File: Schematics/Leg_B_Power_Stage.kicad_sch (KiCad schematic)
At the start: 40 parts, among them Q4 C3M0025065K, Q5 C3M0025065K, U3 UCC21710QDWRQ1, U4 UCC21710QDWRQ1

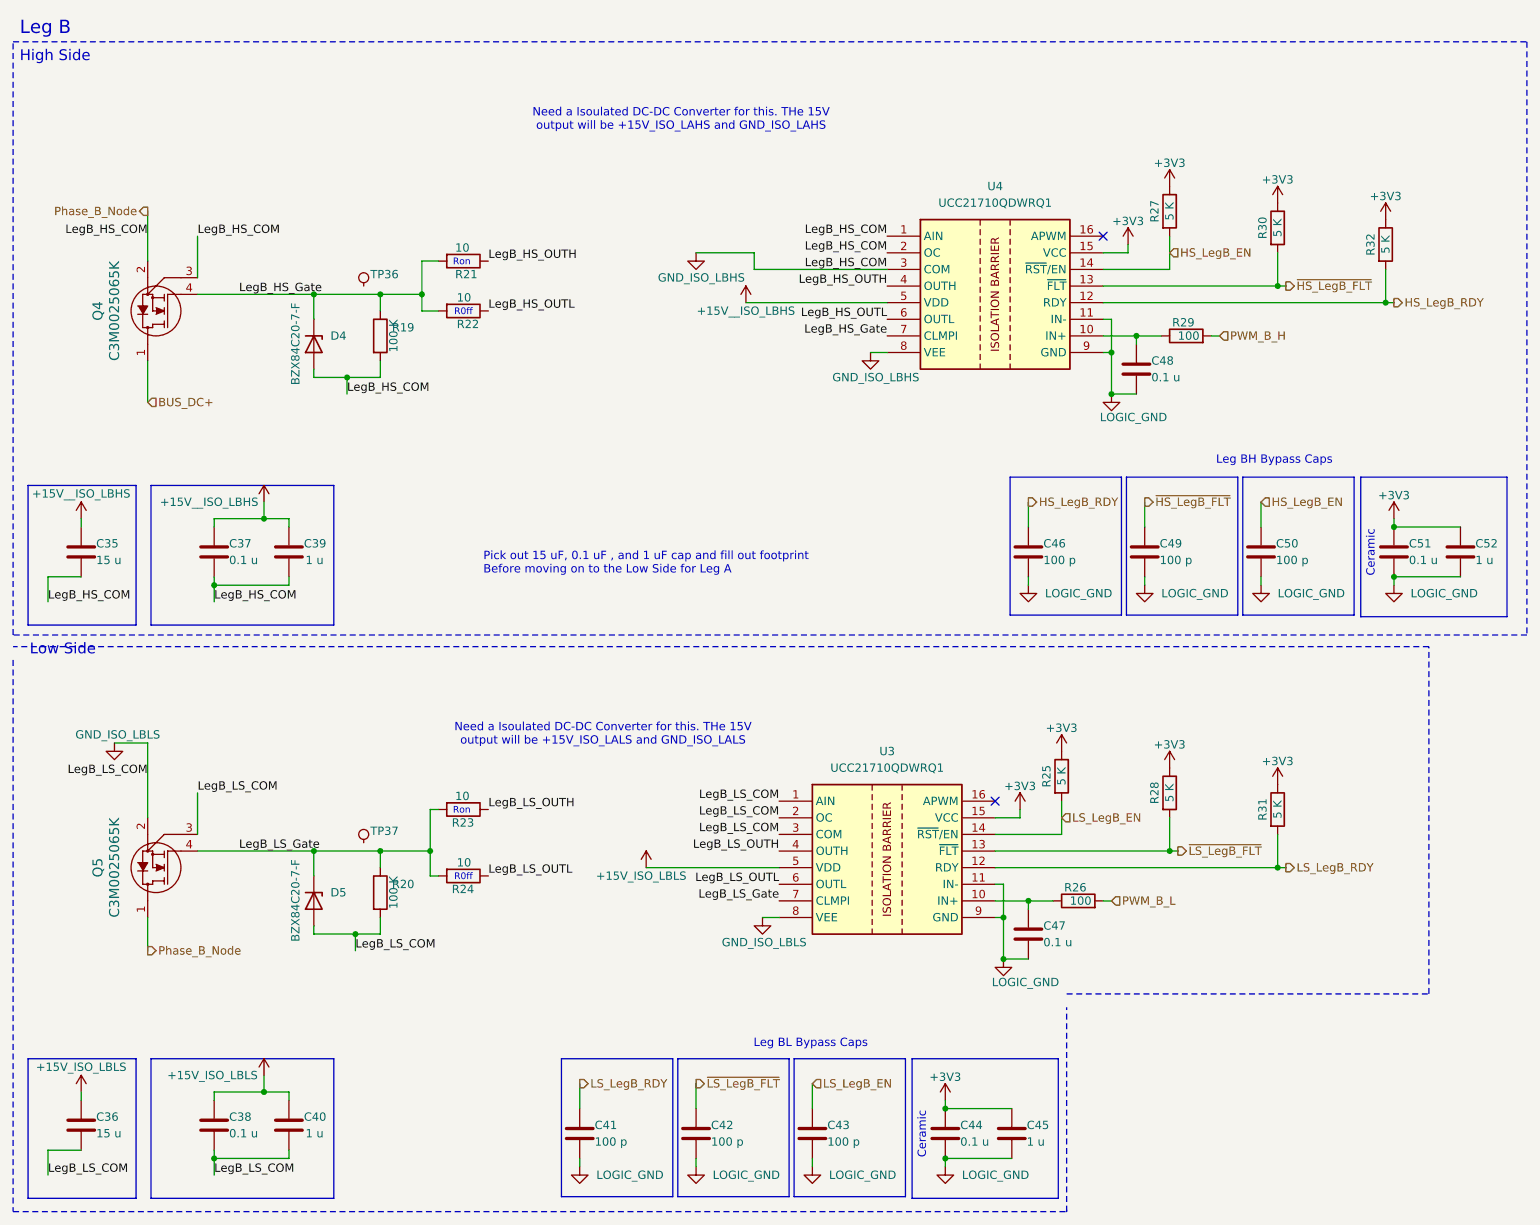
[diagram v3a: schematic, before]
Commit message: Changing units on all Caps to display xF
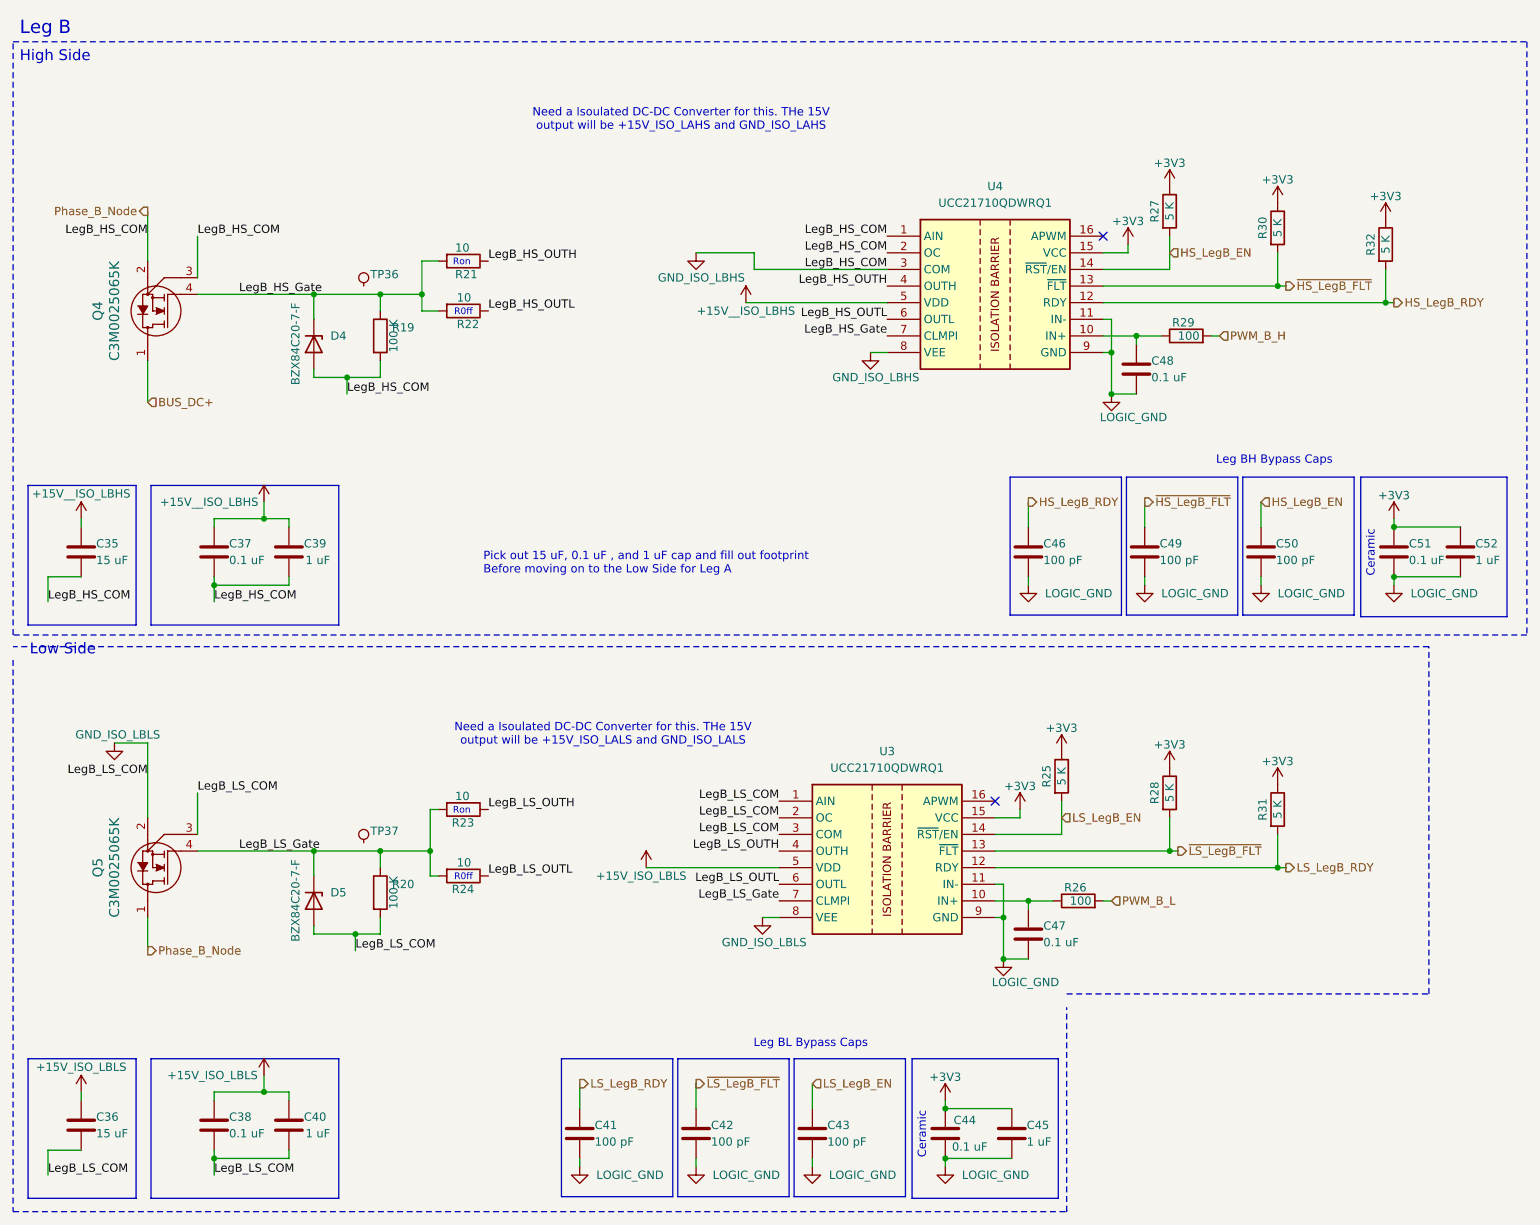
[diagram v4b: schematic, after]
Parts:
- C35, C36: value 15 u -> 15 uF
- C37, C38, C44, C47, C48, C51: value 0.1 u -> 0.1 uF
- C39, C40, C45, C52: value 1 u -> 1 uF
- C41, C42, C43, C46, C49, C50: value 100 p -> 100 pF
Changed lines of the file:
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@@
 	(rectangle
 		(start 34.798 83.82)
-		(end 62.738 105.156)
+		(end 63.5 105.156)
 		(stroke
 			(width 0)
@@
 	(rectangle
 		(start 34.798 171.45)
-		(end 62.738 192.786)
+		(end 63.5 192.786)
 		(stroke
 			(width 0)
@@
 			)
 		)
-		(property "Value" "100 p"
+		(property "Value" "100 pF"
 			(at 138.176 184.15 0)
 			(effects
@@
 			)
 		)
-		(property "Value" "100 p"
+		(property "Value" "100 pF"
 			(at 171.196 95.25 0)
 			(effects
@@
 			)
 		)
-		(property "Value" "15 u"
+		(property "Value" "15 uF"
 			(at 26.416 182.88 0)
 			(effects
@@
 			)
 		)
-		(property "Value" "0.1 u"
+		(property "Value" "0.1 uF"
 			(at 46.736 95.25 0)
 			(effects
@@
 			)
 		)
-		(property "Value" "100 p"
+		(property "Value" "100 pF"
 			(at 206.756 95.25 0)
 			(effects
@@
 			)
 		)
-		(property "Value" "1 u"
+		(property "Value" "1 uF"
 			(at 168.656 184.15 0)
 			(effects
@@
 			)
 		)
-		(property "Value" "1 u"
+		(property "Value" "1 uF"
 			(at 58.42 95.25 0)
 			(effects
@@
 		(dnp no)
 		(property "Reference" "C44"
-			(at 158.496 181.61 0)
+			(at 157.48 180.848 0)
 			(effects
 				(font
@@
 			)
 		)
-		(property "Value" "0.1 u"
-			(at 158.496 184.15 0)
+		(property "Value" "0.1 uF"
+			(at 157.226 184.912 0)
 			(effects
 				(font
@@
 			)
 		)
-		(property "Value" "0.1 u"
+		(property "Value" "0.1 uF"
 			(at 46.736 182.88 0)
 			(effects
@@
 			)
 		)
-		(property "Value" "1 u"
+		(property "Value" "1 uF"
 			(at 58.42 182.88 0)
 			(effects
@@
 			)
 		)
-		(property "Value" "100 p"
+		(property "Value" "100 pF"
 			(at 120.396 184.15 0)
 			(effects
@@
 			)
 		)
-		(property "Value" "0.1 u"
+		(property "Value" "0.1 uF"
 			(at 187.706 67.31 0)
 			(effects
@@
 			)
 		)
-		(property "Value" "15 u"
+		(property "Value" "15 uF"
 			(at 26.416 95.25 0)
 			(effects
@@
 			)
 		)
-		(property "Value" "100 p"
+		(property "Value" "100 pF"
 			(at 188.976 95.25 0)
 			(effects
@@
 			)
 		)
-		(property "Value" "1 u"
+		(property "Value" "1 uF"
 			(at 237.236 95.25 0)
 			(effects
@@
 			)
 		)
-		(property "Value" "0.1 u"
+		(property "Value" "0.1 uF"
 			(at 227.076 95.25 0)
 			(effects
@@
 			)
 		)
-		(property "Value" "0.1 u"
+		(property "Value" "0.1 uF"
 			(at 171.196 153.67 0)
 			(effects
@@
 			)
 		)
-		(property "Value" "100 p"
+		(property "Value" "100 pF"
 			(at 102.616 184.15 0)
 			(effects

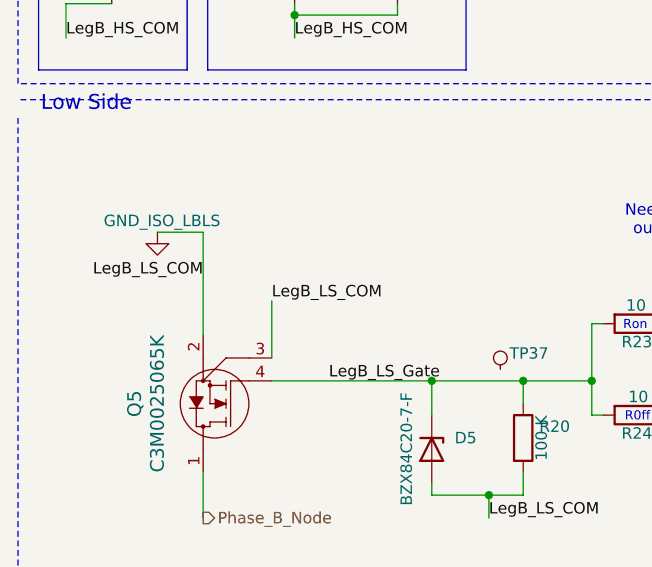
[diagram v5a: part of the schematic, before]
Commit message: Fixing Full Bridge MOSFET ISO_GND to reference GND or DC-
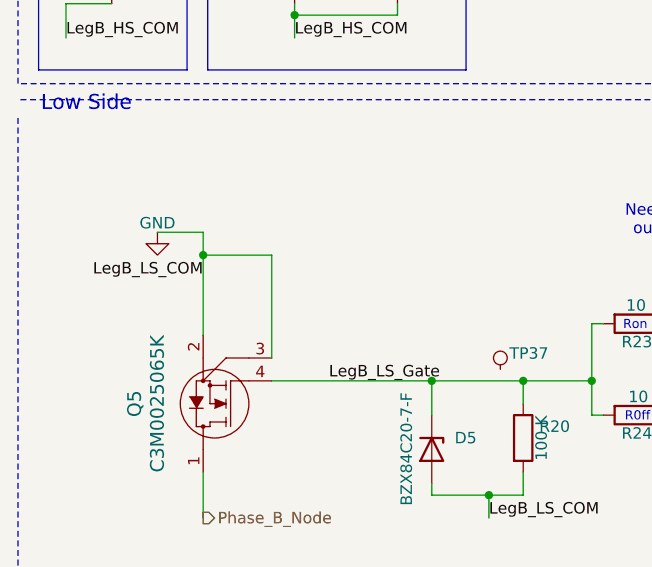
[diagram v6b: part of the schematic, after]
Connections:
- net GND_ISO_LBLS: no longer C36.2, C38.2, C40.2, D5.2 (A), Q5.2, Q5.3, R20.2, U3.1 (AIN), U3.2 (OC), U3.3 (COM)
- new net GND: C36.2, C38.2, C40.2, D5.2 (A), Q5.2, Q5.3, R20.2, U3.1 (AIN), U3.2 (OC), U3.3 (COM)
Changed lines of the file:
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@@
 	)
 	(junction
+		(at 34.29 125.73)
+		(diameter 0)
+		(color 0 0 0 0)
+	)
+	(junction
 		(at 207.01 142.24)
 		(diameter 0)
@@
 	(wire
 		(pts
+			(xy 41.91 125.73) (xy 34.29 125.73)
+		)
+		(stroke
+			(width 0)
+			(type default)
+		)
+	)
+	(wire
+		(pts
 			(xy 34.29 71.12) (xy 34.29 64.77)
 		)
@@
 	(wire
 		(pts
+			(xy 34.29 125.73) (xy 34.29 134.62)
+		)
+		(stroke
+			(width 0)
+			(type default)
+		)
+	)
+	(wire
+		(pts
 			(xy 224.79 88.9) (xy 224.79 90.17)
 		)
@@
 	(wire
 		(pts
-			(xy 34.29 123.19) (xy 34.29 134.62)
+			(xy 34.29 123.19) (xy 34.29 125.73)
 		)
 		(stroke
@@
 	(wire
 		(pts
-			(xy 41.91 130.81) (xy 41.91 137.16)
+			(xy 41.91 125.73) (xy 41.91 137.16)
 		)
 		(stroke
@@
 		)
 	)
-	(label "LegB_LS_COM"
-		(at 41.91 130.81 0)
-		(effects
-			(font
-				(size 1.27 1.27)
-			)
-			(justify left bottom)
-		)
-	)
 	(label "LegB_HS_COM"
 		(at 147.32 45.72 180)
@@
 	(symbol
 		(lib_id "power:GNDS")
-		(at 29.21 123.19 0)
-		(unit 1)
-		(body_style 1)
-		(exclude_from_sim no)
-		(in_bom yes)
-		(on_board yes)
-		(in_pos_files yes)
-		(dnp no)
-		(property "Reference" "#PWR053"
-			(at 29.21 129.54 0)
-			(hide yes)
-			(show_name no)
-			(do_not_autoplace no)
-			(effects
-				(font
-					(size 1.27 1.27)
-				)
-			)
-		)
-		(property "Value" "GND_ISO_LBLS"
-			(at 29.718 121.92 0)
-			(show_name no)
-			(do_not_autoplace no)
-			(effects
-				(font
-					(size 1.27 1.27)
-				)
-			)
-		)
-		(property "Footprint" ""
-			(at 29.21 123.19 0)
-			(hide yes)
-			(show_name no)
-			(do_not_autoplace no)
-			(effects
-				(font
-					(size 1.27 1.27)
-				)
-			)
-		)
-		(property "Datasheet" ""
-			(at 29.21 123.19 0)
-			(hide yes)
-			(show_name no)
-			(do_not_autoplace no)
-			(effects
-				(font
-					(size 1.27 1.27)
-				)
-			)
-		)
-		(property "Description" "Power symbol creates a global label with name \"GNDS\" , signal ground"
-			(at 29.21 123.19 0)
-			(hide yes)
-			(show_name no)
-			(do_not_autoplace no)
-			(effects
-				(font
-					(size 1.27 1.27)
-				)
-			)
-		)
-		(pin "1"
-		)
-		(instances
-			(project "Leg_B_Power_Stage"
-				(path "/0d38f9bf-13f4-4f42-8a58-3b8cdf8f95a0"
-					(reference "#PWR03")
-					(unit 1)
-				)
-			)
-			(project "SiC_Single_Phase_Inverter"
-				(path "/a1ed0539-9735-4ad1-a8fd-87e26e7fce16/b6e78e1f-718a-4f31-892b-d9c389541b0d/d1761b4e-8a42-4386-8dfd-35f782fbcef3"
-					(reference "#PWR053")
-					(unit 1)
-				)
-			)
-		)
-	)
-	(symbol
-		(lib_id "power:GNDS")
 		(at 128.27 149.86 0)
 		(unit 1)
@@
 					(unit 1)
 				)
+			)
+		)
+	)
+	(symbol
+		(lib_id "power:GND")
+		(at 29.21 123.19 0)
+		(unit 1)
+		(body_style 1)
+		(exclude_from_sim no)
+		(in_bom yes)
+		(on_board yes)
+		(in_pos_files yes)
+		(dnp no)
+		(property "Reference" "#PWR053"
+			(at 29.21 129.54 0)
+			(hide yes)
+			(show_name no)
+			(do_not_autoplace no)
+			(effects
+				(font
+					(size 1.27 1.27)
+				)
+			)
+		)
+		(property "Value" "GND"
+			(at 29.21 122.174 0)
+			(show_name no)
+			(do_not_autoplace no)
+			(effects
+				(font
+					(size 1.27 1.27)
+				)
+			)
+		)
+		(property "Footprint" ""
+			(at 29.21 123.19 0)
+			(hide yes)
+			(show_name no)
+			(do_not_autoplace no)
+			(effects
+				(font
+					(size 1.27 1.27)
+				)
+			)
+		)
+		(property "Datasheet" ""
+			(at 29.21 123.19 0)
+			(hide yes)
+			(show_name no)
+			(do_not_autoplace no)
+			(effects
+				(font
+					(size 1.27 1.27)
+				)
+			)
+		)
+		(property "Description" "Power symbol creates a global label with name \"GND\" , ground"
+			(at 29.21 123.19 0)
+			(hide yes)
+			(show_name no)
+			(do_not_autoplace no)
+			(effects
+				(font
+					(size 1.27 1.27)
+				)
+			)
+		)
+		(pin "1"
+		)
+		(instances
+			(project "SiC_Single_Phase_Inverter"
+				(path "/a1ed0539-9735-4ad1-a8fd-87e26e7fce16/b6e78e1f-718a-4f31-892b-d9c389541b0d/d1761b4e-8a42-4386-8dfd-35f782fbcef3"
+					(reference "#PWR053")
+					(unit 1)
+				)
